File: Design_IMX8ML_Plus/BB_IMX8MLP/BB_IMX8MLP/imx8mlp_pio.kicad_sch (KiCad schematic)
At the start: 2 parts, among them J3 DF40C-100DP-0.4V_51_, J4 DF40C-100DP-0.4V_51_

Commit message: Add Base board IMxM8ML project
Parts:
- added J1, J2: DF40C-100DP-0.4V_51_, _W_SBC:HIROSE_DF40C-100DS-0.4V_51_, symbol CONN_DF40C-100DS-0_4V51_HIR:DF40C-100DP-0.4V_51_
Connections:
- net CSI1_CLK_N: no longer names the net of J3.67
- net CSI1_CLK_P: no longer names the net of J3.65
- net CSI2_CLK_N: no longer names the net of J3.73
- net CSI2_CLK_P: no longer names the net of J3.71
- net DSI1_CLK_N: no longer names the net of J3.79
- net DSI1_CLK_P: no longer names the net of J3.77
- net EARC_AUX: no longer names the net of J3.85
- net EARC_N_HPD: no longer names the net of J3.87
- net EARC_P_UTIL: no longer names the net of J3.89
- net ECSPI1_MISO: no longer names the net of J3.80
- net ECSPI1_MOSI: no longer names the net of J3.82
- net ECSPI1_SCLK: no longer names the net of J3.84
- net ECSPI1_SSO: no longer names the net of J3.86
- net ECSPI2_MISO: no longer names the net of J3.88
- net ECSPI2_MOSI: no longer names the net of J3.90
- net ECSPI2_SCLK: no longer names the net of J3.92
- net ECSPI2_SSO: no longer names the net of J3.94
- net I2C1_SCL: no longer names the net of J3.21
- net I2C1_SDA: no longer names the net of J3.23
- net I2C2_SCL: no longer names the net of J3.33
- net I2C2_SDA: no longer names the net of J3.35
- net I2C3_SCL: no longer names the net of J3.29
- net I2C3_SDA: no longer names the net of J3.27
- net I2C4_SCL: no longer names the net of J3.41
- net I2C4_SDA: no longer names the net of J3.39
- net LED1: no longer names the net of J4.60
- net LED2: no longer names the net of J4.62
- net SAI1_MCLK: no longer names the net of J3.11
- net SAI1_RXC: no longer names the net of J3.13
- net SAI1_RXD0: no longer names the net of J3.48
- net SAI1_RXD1: no longer names the net of J3.50
- net SAI1_RXD2: no longer names the net of J3.52
- net SAI1_RXD3: no longer names the net of J3.54
- net SAI1_RXD4: no longer names the net of J3.56
- net SAI1_RXD5: no longer names the net of J4.29
- net SAI1_RXD6: no longer names the net of J4.31
- net SAI1_RXD7: no longer names the net of J4.33
- net SAI1_RXD7: no longer J4.49
- net SAI1_RXFS: no longer names the net of J3.15
- net SAI1_TXC: no longer names the net of J3.17
- net SAI1_TXD0: no longer names the net of J4.35
- net SAI1_TXD1: no longer names the net of J4.37
- net SAI1_TXD2: no longer names the net of J4.39
- net SAI1_TXD3: no longer names the net of J4.41
- net SAI1_TXD4: no longer names the net of J4.43
- net SAI1_TXD5: no longer names the net of J4.45
- net SAI1_TXD6: no longer names the net of J4.47
- net SAI2_MCLK: no longer names the net of J3.10
- net SAI2_RXC: no longer names the net of J3.12
- net SAI2_RXD0: no longer names the net of J3.22
- net SAI2_RXFS: no longer names the net of J3.14
- net SAI2_TXC: no longer names the net of J3.16
- net SAI2_TXD0: no longer names the net of J3.24
- net SAI2_TXFS: no longer names the net of J3.18
- net SAI3_MCLK: no longer names the net of J3.28
- net SAI3_RXC: no longer names the net of J3.30
- net SAI3_RXD: no longer names the net of J3.32
- net SAI3_RXFS: no longer names the net of J3.34
- net SAI3_TXC: no longer names the net of J3.36
- net SAI3_TXD: no longer names the net of J3.38
- net SAI3_TXFS: no longer names the net of J3.40
- net SAI5_MCLK: no longer names the net of J4.40
- net SAI5_RXC: no longer names the net of J4.42
- net SAI5_RXD0: no longer names the net of J4.32
- net SAI5_RXD1: no longer names the net of J4.34
- net SAI5_RXD2: no longer names the net of J4.36
- net SAI5_RXD3: no longer names the net of J4.38
- net SAI5_RXFS: no longer names the net of J4.44
- net SAi1_TXFS: no longer names the net of J3.19
- net TXRXA_N: no longer names the net of J4.66
- net TXRXA_P: no longer names the net of J4.68
- net TXRXB_N: no longer names the net of J4.72
- net TXRXB_P: no longer names the net of J4.74
- net TXRXC_N: no longer names the net of J4.80
- net TXRXC_P: no longer names the net of J4.78
- net TXRXD_N: no longer names the net of J4.84
- net TXRXD_P: no longer names the net of J4.86
- net UART1_RXD: no longer names the net of J3.45
- net UART1_TXD: no longer names the net of J3.47
- net UART2_RXD: no longer names the net of J3.49
- net UART2_TXD: no longer names the net of J3.51
- net UART3_RXD: no longer names the net of J3.53
- net UART3_TXD: no longer names the net of J3.55
- net UART4_RXD: no longer names the net of J3.57
- net UART4_TXD: no longer names the net of J3.59

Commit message: Add SPB228 WIFI/BLE module
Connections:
- net SAI2_MCLK: now reaches J2.10
- net SAI1_MCLK: now reaches J2.11
- net SAI2_RXC: now reaches J2.12
- net SAI1_RXC: now reaches J2.13
- net SAI2_RXFS: now reaches J2.14
- net SAI1_RXFS: now reaches J2.15
- net SAI2_TXC: now reaches J2.16
- net SAI1_TXC: now reaches J2.17
- net SAI2_TXFS: now reaches J2.18
- net SAi1_TXFS: now reaches J2.19
- net I2C1_SCL: now reaches J2.21
- net SAI2_RXD0: now reaches J2.22
- net I2C1_SDA: now reaches J2.23
- net SAI2_TXD0: now reaches J2.24
- net I2C3_SDA: now reaches J2.27
- net SAI3_MCLK: now reaches J2.28
- net I2C3_SCL: now reaches J2.29
- net SAI3_RXC: now reaches J2.30
- net SAI3_RXD: now reaches J2.32
- net I2C2_SCL: now reaches J2.33
- net SAI3_RXFS: now reaches J2.34
- net I2C2_SDA: now reaches J2.35
- net SAI3_TXC: now reaches J2.36
- net SAI3_TXD: now reaches J2.38
- net I2C4_SDA: now reaches J2.39
- net SAI3_TXFS: now reaches J2.40
- net I2C4_SCL: now reaches J2.41
- net UART1_RXD: now reaches J2.45
- net UART1_TXD: now reaches J2.47
- net SAI1_RXD0: now reaches J2.48
- net UART2_RXD: now reaches J2.49
- net SAI1_RXD1: now reaches J2.50
- net UART2_TXD: now reaches J2.51
- net SAI1_RXD2: now reaches J2.52
- net UART3_RXD: now reaches J2.53
- net SAI1_RXD3: now reaches J2.54
- net UART3_TXD: now reaches J2.55
- net SAI1_RXD4: now reaches J2.56
- net UART4_RXD: now reaches J2.57
- net UART4_TXD: now reaches J2.59
- net CSI1_CLK_P: now reaches J2.65
- net CSI1_CLK_N: now reaches J2.67
- net CSI2_CLK_P: now reaches J2.71
- net CSI2_CLK_N: now reaches J2.73
- net DSI1_CLK_P: now reaches J2.77
- net DSI1_CLK_N: now reaches J2.79
- net ECSPI1_MISO: now reaches J2.80
- net ECSPI1_MOSI: now reaches J2.82
- net ECSPI1_SCLK: now reaches J2.84
- net EARC_AUX: now reaches J2.85
- net ECSPI1_SSO: now reaches J2.86
- net EARC_N_HPD: now reaches J2.87
- net ECSPI2_MISO: now reaches J2.88
- net EARC_P_UTIL: now reaches J2.89
- net ECSPI2_MOSI: now reaches J2.90
- net ECSPI2_SCLK: now reaches J2.92
- net ECSPI2_SSO: now reaches J2.94
- net VDD_SYS: now reaches J3.100
- net VDD_SYS: now also J3.89, J3.90, J3.91, J3.92, J3.93, J3.94, J3.95, J3.96, J3.97, J3.98, J3.99
- net PCIE_TXN_P: now reaches J3.11
- net PCIE_TXN_N: now reaches J3.13
- net PCIE_RXN_P: now reaches J3.15
- net PCIE_RXN_N: now reaches J3.17
- net PCIE_REF_PAD_CLK_P: now reaches J3.21
- net PCIE_REF_PAD_CLK_N: now reaches J3.23
- net GPIO1_IO00: now reaches J3.33
- net GPIO1_IO01: now reaches J3.35
- net GPIO1_IO02: now reaches J3.37
- net GPIO1_IO05: now reaches J3.43
- net GPIO1_IO06: now reaches J3.45
- net GPIO1_IO07: now reaches J3.47
- net GPIO1_IO08: now reaches J3.49
- net GPIO1_IO09: now reaches J3.51
- net GPIO1_IO10: now reaches J3.53
- net GPIO1_IO11: now reaches J3.55
- net GPIO1_IO12: now reaches J3.57
- net GPIO1_IO13: now reaches J3.59
- net GPIO1_IO14: now reaches J3.61
- net GPIO1_IO15: now reaches J3.63
- net GND: now reaches J3.75
- net GND: now also J3.76, J3.77, J3.78, J3.79, J3.80, J3.81, J3.82, J3.83, J3.84, J3.85, J3.86, J3.87, J3.88
- net JTAG_TMS: now reaches J4.10
- net HDM_TX2_N: now reaches J4.11
- net JTAG_TDO: now reaches J4.12
- net HDM_TX1_P: now reaches J4.13
- net JTAG_TDI: now reaches J4.14
- net HDM_TX1_N: now reaches J4.15
- net JTAG_TCK: now reaches J4.16
- net HDM_TX0_P: now reaches J4.17
- net JTAG_MOD: now reaches J4.18
- net HDM_TX0_N: now reaches J4.19
- net CLKOUT2: now reaches J4.22
- net HDM_HPD: now reaches J4.23
- net CLKOUT1: now reaches J4.24
- net HDM_DDC_SDA: now reaches J4.25
- net CLKIN2: now reaches J4.26
- net HDM_DDC_SCL: now reaches J4.27
- net CLKIN1: now reaches J4.28
- net HDM_CEC: now reaches J4.29
- net BOOT_MODE3: now reaches J4.32
- net BOOT_MODE2: now reaches J4.34
- net BOOT_MODE1: now reaches J4.36
- net LVDS1_CLK_N: now reaches J4.37
- net BOOT_MODE0: now reaches J4.38
- net LVDS1_CLK_P: now reaches J4.39
- net LVDS1_D3_P: now reaches J4.41
- net LVDS1_D3_N: now reaches J4.43
- net SDC1_STROBE: now reaches J4.44
- net LVDS1_D2_P: now reaches J4.45
- net SDC1_RESET_B: now reaches J4.46
- net LVDS1_D2_N: now reaches J4.47
- net SDC1_DATA7: now reaches J4.48
- net LVDS1_D1_P: now reaches J4.49
- net HDM_TXC_P: now reaches J4.5
- net SDC1_DATA6: now reaches J4.50
- net LVDS1_D1_N: now reaches J4.51
- net SDC1_DATA5: now reaches J4.52
- net LVDS1_D0_P: now reaches J4.53
- net SDC1_DATA4: now reaches J4.54
- net LVDS1_D0_N: now reaches J4.55
- net SDC1_DATA3: now reaches J4.56
- net SDC1_DATA2: now reaches J4.58
- net LVDS0_CLK_P: now reaches J4.59
- net SDC1_DATA1: now reaches J4.60
- net LVDS0_CLK_N: now reaches J4.61
- net SDC1_DATA0: now reaches J4.62
- net LVDS0_D3_P: now reaches J4.63
- net SDC1_CMD: now reaches J4.64
- net LVDS0_D3_N: now reaches J4.65
- net SDC1_CLK: now reaches J4.66
- net LVDS0_D2_P: now reaches J4.67
- net LVDS0_D2_N: now reaches J4.69
- net HDM_TXC_N: now reaches J4.7
- net SDC2_WP: now reaches J4.70
- net LVDS0_D1_P: now reaches J4.71
- net SDC2_RESET_B: now reaches J4.72
- net LVDS0_D1_N: now reaches J4.73
- net SDC2_DATA3: now reaches J4.74
- net LVDS0_D0_P: now reaches J4.75
- net SDC2_DATA2: now reaches J4.76
- net LVDS0_D0_N: now reaches J4.77
- net SDC2_DATA1: now reaches J4.78
- net SDC2_DATA0: now reaches J4.80
- net SDC2_CMD: now reaches J4.82
- net SDC2_CLK: now reaches J4.84
- net SDC2_CD_B: now reaches J4.86
- net HDM_TX2_P: now reaches J4.9
- net SAI1_RXD5: now reaches J1.29
- net SAI1_RXD6: now reaches J1.31
- net SAI5_RXD0: now reaches J1.32
- net SAI1_RXD7: now reaches J1.33
- net SAI1_RXD7: now also J1.49
- net SAI5_RXD1: now reaches J1.34
- net SAI1_TXD0: now reaches J1.35
- net SAI5_RXD2: now reaches J1.36
- net SAI1_TXD1: now reaches J1.37
- net SAI5_RXD3: now reaches J1.38
- net SAI1_TXD2: now reaches J1.39
- net SAI5_MCLK: now reaches J1.40
- net SAI1_TXD3: now reaches J1.41
- net SAI5_RXC: now reaches J1.42
- net SAI1_TXD4: now reaches J1.43
- net SAI5_RXFS: now reaches J1.44
- net SAI1_TXD5: now reaches J1.45
- net SAI1_TXD6: now reaches J1.47
- net LED1: now reaches J1.60
- net LED2: now reaches J1.62
- net TXRXA_N: now reaches J1.66
- net TXRXA_P: now reaches J1.68
- net TXRXB_N: now reaches J1.72
- net TXRXB_P: now reaches J1.74
- net TXRXC_P: now reaches J1.78
- net TXRXC_N: now reaches J1.80
- net TXRXD_N: now reaches J1.84
- net TXRXD_P: now reaches J1.86

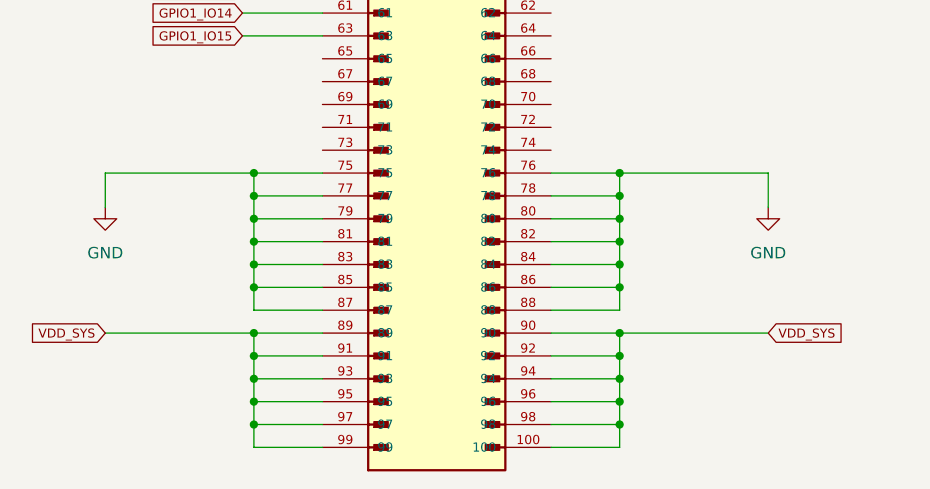
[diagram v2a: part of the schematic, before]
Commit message: Improve power source module in the base board
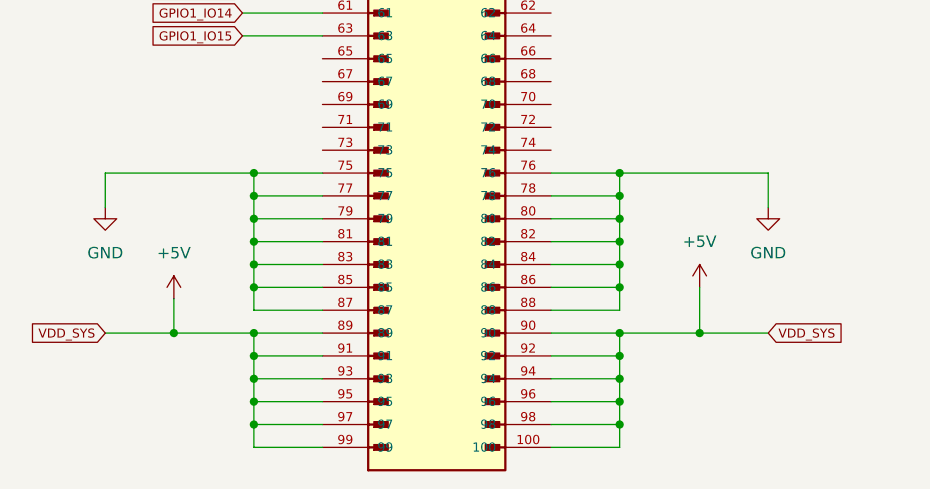
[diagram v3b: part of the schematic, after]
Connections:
- net VDD_SYS renamed +5V
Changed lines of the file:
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@@
 	)
 	(junction
+		(at -104.14 138.43)
+		(diameter 0)
+		(color 0 0 0 0)
+	)
+	(junction
 		(at -54.61 146.05)
 		(diameter 0)
@@
 	)
 	(junction
+		(at -45.72 138.43)
+		(diameter 0)
+		(color 0 0 0 0)
+	)
+	(junction
 		(at -54.61 123.19)
 		(diameter 0)
@@
 	(wire
 		(pts
-			(xy -111.76 138.43) (xy -95.25 138.43)
+			(xy -111.76 138.43) (xy -104.14 138.43)
 		)
 		(stroke
@@
 	(wire
 		(pts
+			(xy -45.72 138.43) (xy -54.61 138.43)
+		)
+		(stroke
+			(width 0)
+			(type default)
+		)
+	)
+	(wire
+		(pts
 			(xy 82.55 96.52) (xy 91.44 96.52)
 		)
@@
 	(wire
 		(pts
+			(xy -104.14 134.62) (xy -104.14 138.43)
+		)
+		(stroke
+			(width 0)
+			(type default)
+		)
+	)
+	(wire
+		(pts
 			(xy -95.25 130.81) (xy -95.25 128.27)
 		)
@@
 	(wire
 		(pts
+			(xy -45.72 133.35) (xy -45.72 138.43)
+		)
+		(stroke
+			(width 0)
+			(type default)
+		)
+	)
+	(wire
+		(pts
 			(xy 57.15 104.14) (xy 48.26 104.14)
 		)
@@
 	(wire
 		(pts
-			(xy -38.1 138.43) (xy -54.61 138.43)
+			(xy -38.1 138.43) (xy -45.72 138.43)
 		)
 		(stroke
@@
 	(wire
 		(pts
+			(xy -104.14 138.43) (xy -95.25 138.43)
+		)
+		(stroke
+			(width 0)
+			(type default)
+		)
+	)
+	(wire
+		(pts
 			(xy -38.1 120.65) (xy -54.61 120.65)
 		)
@@
 	)
 	(symbol
+		(lib_id "power:+5V")
+		(at -45.72 133.35 0)
+		(unit 1)
+		(exclude_from_sim no)
+		(in_bom yes)
+		(on_board yes)
+		(dnp no)
+		(property "Reference" "#PWR038"
+			(at -45.72 137.16 0)
+			(effects
+				(font
+					(size 1.27 1.27)
+				)
+				(hide yes)
+			)
+		)
+		(property "Value" "+5V"
+			(at -45.72 128.27 0)
+			(effects
+				(font
+					(size 1.27 1.27)
+				)
+			)
+		)
+		(property "Footprint" ""
+			(at -45.72 133.35 0)
+			(effects
+				(font
+					(size 1.27 1.27)
+				)
+				(hide yes)
+			)
+		)
+		(property "Datasheet" ""
+			(at -45.72 133.35 0)
+			(effects
+				(font
+					(size 1.27 1.27)
+				)
+				(hide yes)
+			)
+		)
+		(property "Description" "Power symbol creates a global label with name \"+5V\""
+			(at -45.72 133.35 0)
+			(effects
+				(font
+					(size 1.27 1.27)
+				)
+				(hide yes)
+			)
+		)
+		(pin "1"
+		)
+		(instances
+			(project "BB_IMX8MLP"
+				(path "/cd2fb234-91e5-476f-84ed-38419b628dc6/654a2f2f-b0bc-45e1-bc79-3ecb22a05819"
+					(reference "#PWR038")
+					(unit 1)
+				)
+			)
+		)
+	)
+	(symbol
 		(lib_id "CONN_DF40C-100DS-0_4V51_HIR:DF40C-100DP-0.4V_51_")
 		(at 149.86 85.09 0)
@@
 					(unit 1)
 				)
+			)
+		)
+	)
+	(symbol
+		(lib_id "power:+5V")
+		(at -104.14 134.62 0)
+		(unit 1)
+		(exclude_from_sim no)
+		(in_bom yes)
+		(on_board yes)
+		(dnp no)
+		(property "Reference" "#PWR036"
+			(at -104.14 138.43 0)
+			(effects
+				(font
+					(size 1.27 1.27)
+				)
+				(hide yes)
+			)
+		)
+		(property "Value" "+5V"
+			(at -104.14 129.54 0)
+			(effects
+				(font
+					(size 1.27 1.27)
+				)
+			)
+		)
+		(property "Footprint" ""
+			(at -104.14 134.62 0)
+			(effects
+				(font
+					(size 1.27 1.27)
+				)
+				(hide yes)
+			)
+		)
+		(property "Datasheet" ""
+			(at -104.14 134.62 0)
+			(effects
+				(font
+					(size 1.27 1.27)
+				)
+				(hide yes)
+			)
+		)
+		(property "Description" "Power symbol creates a global label with name \"+5V\""
+			(at -104.14 134.62 0)
+			(effects
+				(font
+					(size 1.27 1.27)
+				)
+				(hide yes)
+			)
+		)
+		(pin "1"
+		)
+		(instances
+			(project "BB_IMX8MLP"
+				(path "/cd2fb234-91e5-476f-84ed-38419b628dc6/654a2f2f-b0bc-45e1-bc79-3ecb22a05819"
+					(reference "#PWR036")
+					(unit 1)
+				)

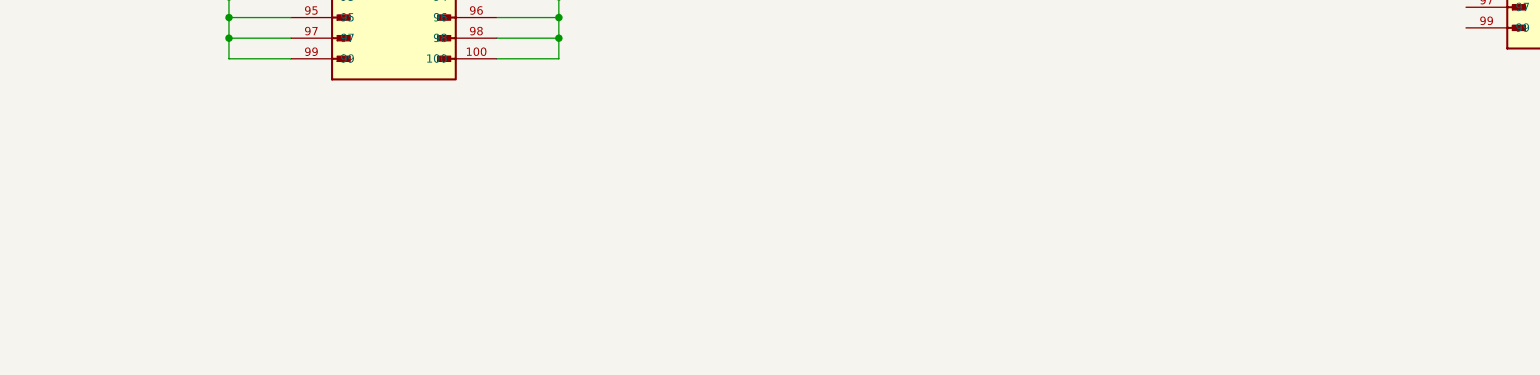
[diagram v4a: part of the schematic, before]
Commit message: Add LVDs and CSI Interface
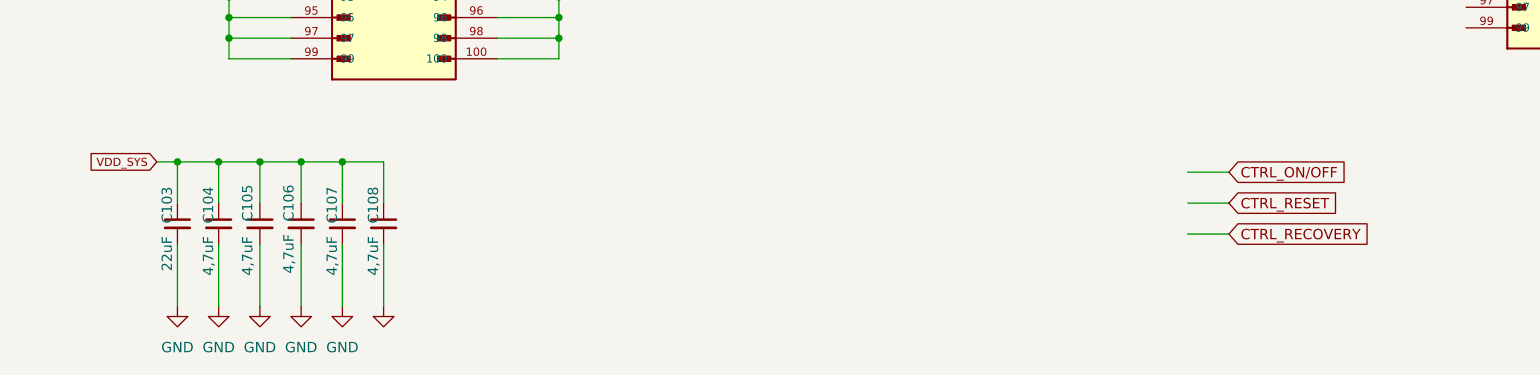
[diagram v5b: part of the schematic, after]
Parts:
- added C103: 22uF, Capacitor_SMD:C_0402_1005Metric, symbol Device:C_Small
- added C104, C105, C106, C107, C108: 4,7uF, Capacitor_SMD:C_0402_1005Metric, symbol Device:C_Small
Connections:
- net +5V: now also C103.1, C104.1, C105.1, C106.1, C107.1, C108.1
- net GND: now also C103.2, C104.2, C105.2, C106.2, C107.2, C108.2

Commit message: reorganization of the componentes
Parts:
- removed J3: DF40C-100DP-0.4V_51_, _W_SBC:HIROSE_DF40C-100DS-0.4V_51_, symbol CONN_DF40C-100DS-0_4V51_HIR:DF40C-100DP-0.4V_51_
- added J3: DF40C-100DP-0.4V_51_, _W_SBC:HIROSE_DF40C-100DS-0.4V_51_, symbol df40c-100dp-0.4v_51_:DF40C-100DP-0.4V_51_
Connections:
- net +5V: now also J3.100, J3.89, J3.90, J3.91, J3.92, J3.93, J3.94, J3.95, J3.96, J3.97, J3.98, J3.99
- net GND: now also J3.75, J3.76, J3.77, J3.78, J3.79, J3.80, J3.81, J3.82, J3.83, J3.84, J3.85, J3.86, J3.87, J3.88
- net LVDS0_CLK_N: no longer J4.61
- net LVDS0_CLK_P: no longer J4.59
- net LVDS0_D0_N: no longer J4.77
- net LVDS0_D0_P: no longer J4.75
- net LVDS0_D1_N: no longer J4.73
- net LVDS0_D1_P: no longer J4.71
- net LVDS0_D2_N: no longer J4.69
- net LVDS0_D2_P: no longer J4.67
- net LVDS0_D3_N: no longer J4.65
- net LVDS0_D3_P: no longer J4.63
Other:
- moved on the sheet: C103, C104, C105, C106, C107, C108, J1, J2, J4
